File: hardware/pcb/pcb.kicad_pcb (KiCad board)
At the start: 2 copper layers, 68.6 x 71.1 mm, 55 parts, among them IC1 ATMEGA32U2, P1 USB, P2 PRGM, SW1 SW_PUSH, U00 MX-DI, U01 MX-DI, U02 MX-DI, U03 MX-DI, U10 MX-DI, U11 MX-DI, U12 MX-DI, U13 MX-DI, U20 MX-DI, U21 MX-DI, U22 MX-DI, U23 MX-DI, U30 MX-DI, U32 MX-DI, U33 MX-DI, Y1 HC49S

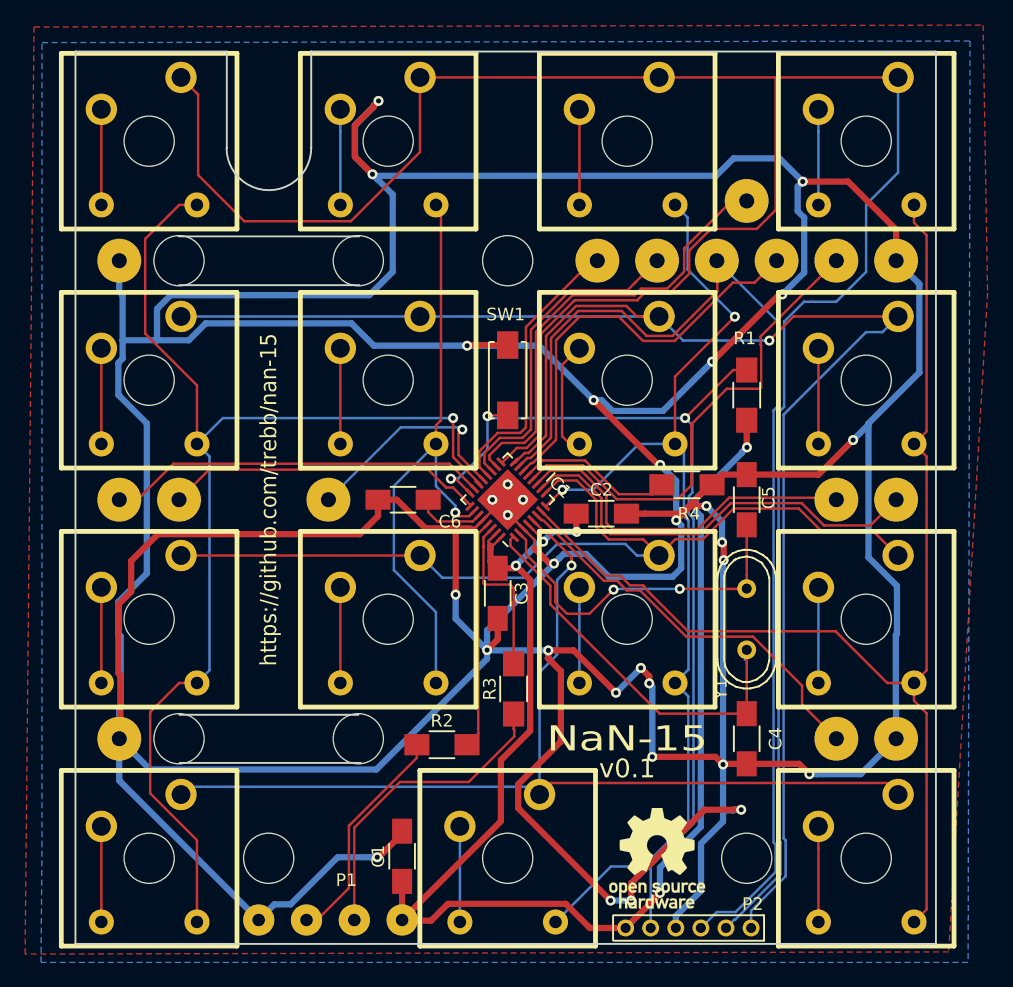
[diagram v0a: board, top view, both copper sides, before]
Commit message: Update version numbers on PCB silkscreens
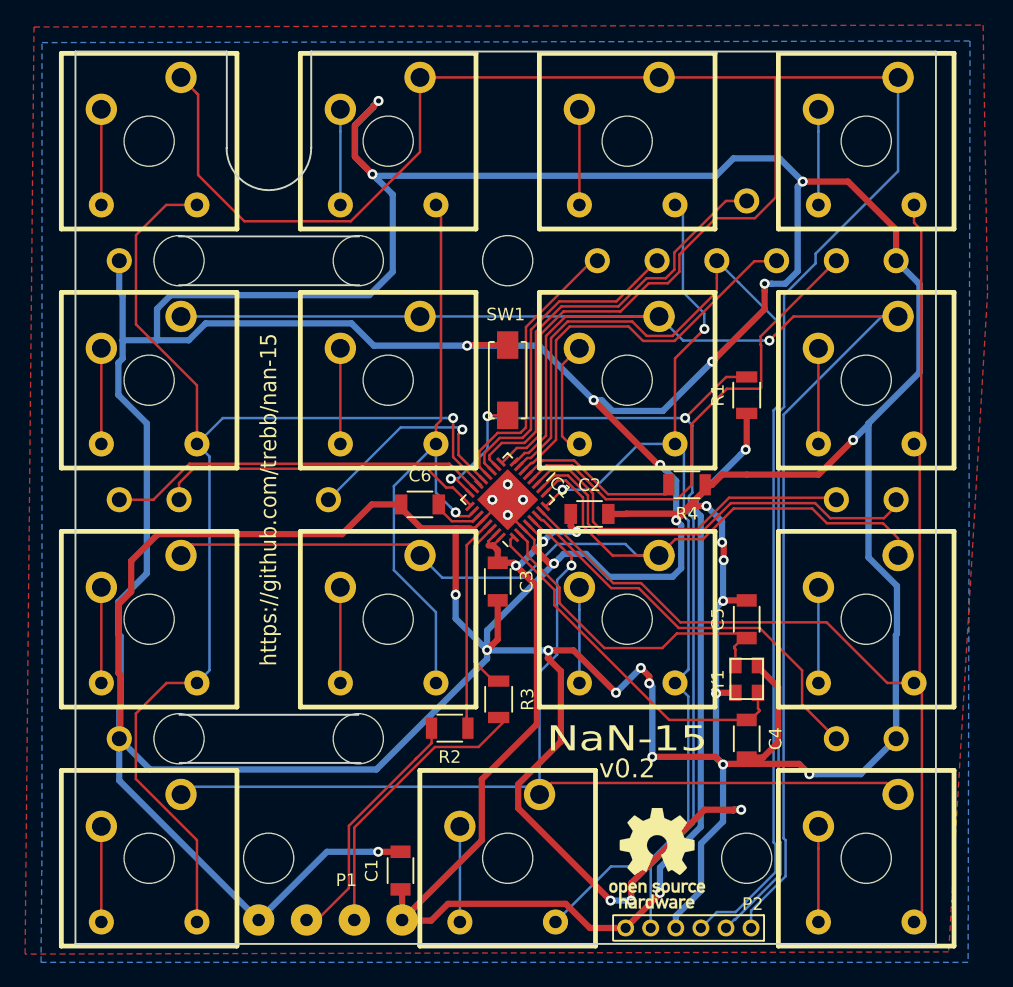
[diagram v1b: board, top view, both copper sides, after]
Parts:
- C1, C2, C3, C4, C5, C6: footprint Capacitors_SMD:C_1206_HandSoldering -> Capacitors_SMD:C_1206
- R1, R2, R3, R4: footprint Resistors_SMD:R_1206_HandSoldering -> Resistors_SMD:R_1206
- W0, W1, W10, W11, W2, W3, W4, W5, W50, W51, W52, W53, W6, W7, W8, W9: footprint nan-15:SolderWirePad_single_1-2mmDrill_no_legend -> nan-15:SolderWirePad_2mm_1-2mmDrill_no_legend
- Y1: value HC49S -> MT 16MHz; footprint Crystals:Crystal_HC49-U_Vertical -> nan-15:crystal_MT_32x25
- moved C5 9.53 mm to (169.1, 111.9)
- moved Y1 4.76 mm to (169.1, 116.7)
- moved R2 1.46 mm to (145.4, 120.6)
- moved R3 1.45 mm to (149.3, 118.3)
- moved C6 1.39 mm to (143.0, 102.8)
- moved C1 1.15 mm to (141.5, 132.0)
- moved C2 0.94 mm to (156.5, 103.5)
- moved C3 0.94 mm to (149.2, 108.9)
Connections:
- net Net-(IC1-Pad29) renamed /D+
- net Net-(IC1-Pad30) renamed /D-
- Y1 pad 1: Net-(C4-Pad1) -> Net-(Y1-Pad1)
- Y1 pad 2: Net-(C5-Pad1) -> Net-(Y1-Pad2)
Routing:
- net GND: track 575.3 -> 590.0 mm, vias 31 -> 33
- net Net-(C4-Pad1): track 32.0 -> 27.9 mm
- net Net-(C5-Pad1): track 28.3 -> 25.5 mm, vias 2 -> 0
- net /col0: track 93.7 -> 96.4 mm
- net /row0: track 195.5 -> 193.1 mm
- net /col2: track 80.9 -> 78.9 mm
- net /D+: track 18.4 -> 16.4 mm
- net Net-(P1-Pad3): track 18.1 -> 20.1 mm
- net Net-(P1-Pad2): track 24.9 -> 23.3 mm
- net /row2: track 76.2 -> 77.7 mm
- net Net-(Y1-Pad2): track 0.00 -> 1.26 mm
- net Net-(Y1-Pad1): track 0.00 -> 1.26 mm
- net /col3: track 95.1 -> 94.0 mm
- net Net-(IC1-Pad13): track 12.7 -> 13.6 mm
- net /led10: track 25.4 -> 26.3 mm
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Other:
- board text added: "v0.2"
- board text removed: "v0.1"

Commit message: Various PCB edits
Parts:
- removed HS4, HS5, HS6, HS7: HEATSINK, nan-15:Plain_Hole_4mm
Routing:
- net /col0: track 96.4 -> 97.8 mm
- net /row1: track 134.2 -> 135.3 mm
- net /col1: track 49.5 -> 50.5 mm
- net Net-(C4-Pad1): track 27.9 -> 27.2 mm
- net Net-(C5-Pad1): track 25.5 -> 24.8 mm
- net /row0: track 193.1 -> 193.7 mm
- net /led7: track 26.5 -> 25.9 mm
- net /led8: track 22.7 -> 22.1 mm
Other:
- outline, holes or cut-outs redrawn
